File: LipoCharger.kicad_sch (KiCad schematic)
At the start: 31 parts, among them J1 S2B-XH-A, J2 USB_C_Receptacle_USB2.0_14P, Q1 2300A, Q2 2300A, SW1 SK12D07VG4, U1 TP4056-42-ESOP8, U2 MT3608, U3 FM2113

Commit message: Fixed ERC errors
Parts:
- renumbered GND1 to GND_OUT1, +5v1 to PWR_OUT1
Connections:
- net +5V: no longer names the net of C5.1, D3.1 (K), PWR_OUT1.1, R10.1
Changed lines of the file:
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@@
 	(wire
 		(pts
-			(xy 83.82 64.77) (xy 83.82 63.5)
-		)
-		(stroke
-			(width 0)
-			(type default)
-		)
-	)
-	(wire
-		(pts
 			(xy 39.37 160.02) (xy 45.72 160.02)
 		)
@@
 		(on_board yes)
 		(dnp no)
-		(property "Reference" "+5v1"
-			(at 259.588 29.464 90)
+		(property "Reference" "PWR_OUT1"
+			(at 257.302 29.464 90)
 			(effects
 				(font
@@
 			(project ""
 				(path "/b34478b6-339b-4f78-905c-fce6e8fbd016"
-					(reference "+5v1")
+					(reference "PWR_OUT1")
 					(unit 1)
 				)
@@
 	)
 	(symbol
-		(lib_id "power:+5V")
-		(at 252.73 33.02 0)
-		(unit 1)
-		(exclude_from_sim no)
-		(in_bom yes)
-		(on_board yes)
-		(dnp no)
-		(fields_autoplaced yes)
-		(property "Reference" "#PWR014"
-			(at 252.73 36.83 0)
-			(effects
-				(font
-					(size 1.27 1.27)
-				)
-				(hide yes)
-			)
-		)
-		(property "Value" "+5V"
-			(at 252.73 27.94 0)
-			(effects
-				(font
-					(size 1.27 1.27)
-				)
-			)
-		)
-		(property "Footprint" ""
-			(at 252.73 33.02 0)
-			(effects
-				(font
-					(size 1.27 1.27)
-				)
-				(hide yes)
-			)
-		)
-		(property "Datasheet" ""
-			(at 252.73 33.02 0)
-			(effects
-				(font
-					(size 1.27 1.27)
-				)
-				(hide yes)
-			)
-		)
-		(property "Description" "Power symbol creates a global label with name \"+5V\""
-			(at 252.73 33.02 0)
-			(effects
-				(font
-					(size 1.27 1.27)
-				)
-				(hide yes)
-			)
-		)
-		(pin "1"
-		)
-		(instances
-			(project ""
-				(path "/b34478b6-339b-4f78-905c-fce6e8fbd016"
-					(reference "#PWR014")
-					(unit 1)
-				)
-			)
-		)
-	)
-	(symbol
 		(lib_id "Device:R")
 		(at 147.32 31.75 0)
@@
 		(on_board yes)
 		(dnp no)
-		(property "Reference" "GND1"
-			(at 259.588 53.594 90)
+		(property "Reference" "GND_OUT1"
+			(at 257.556 53.594 90)
 			(effects
 				(font
@@
 			(project "LipoCharger"
 				(path "/b34478b6-339b-4f78-905c-fce6e8fbd016"
-					(reference "GND1")
+					(reference "GND_OUT1")
 					(unit 1)
 				)

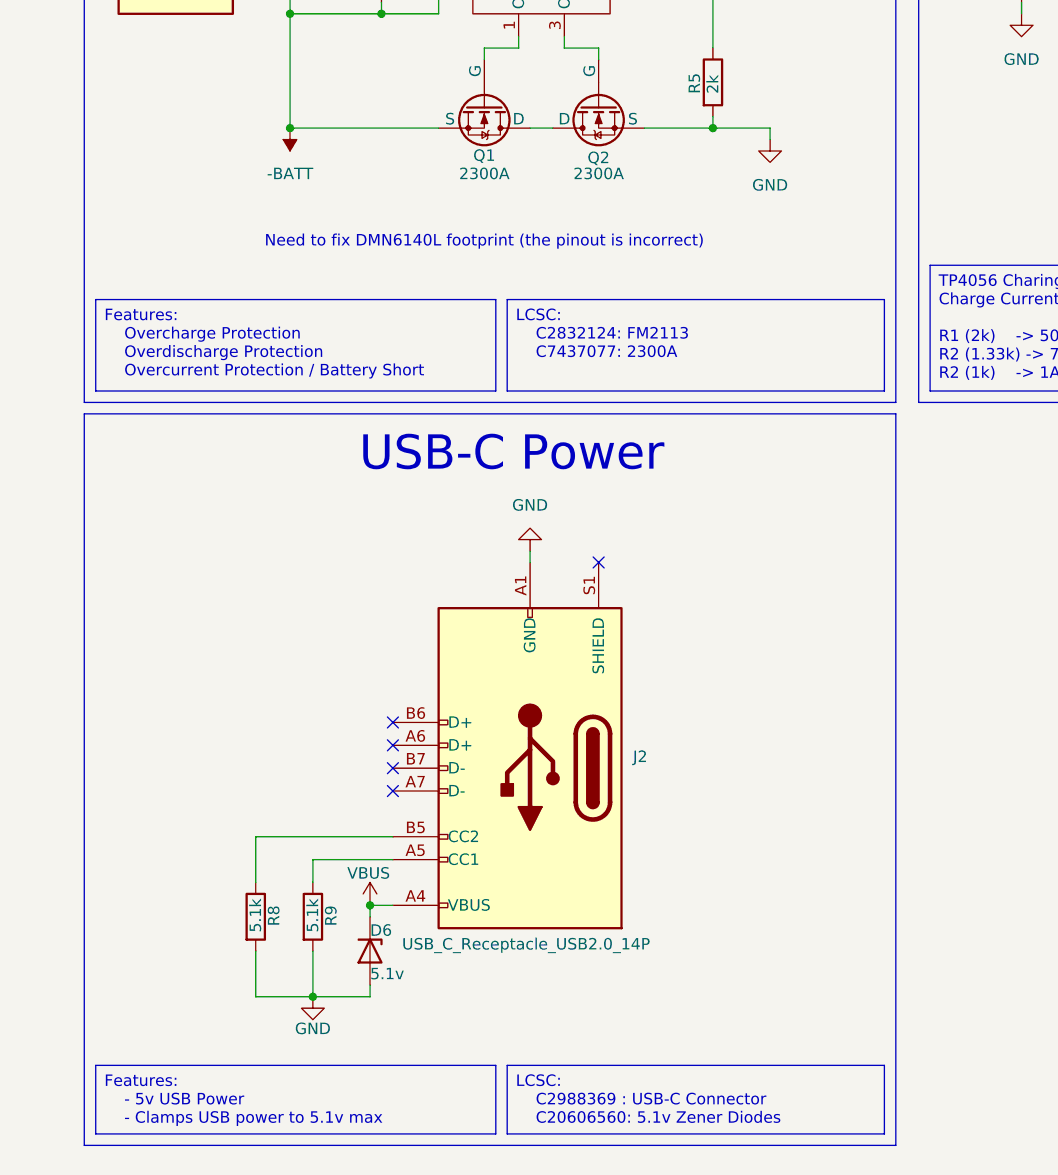
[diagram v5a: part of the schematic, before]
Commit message: updated part numbers to add stock, added part numbers to each part
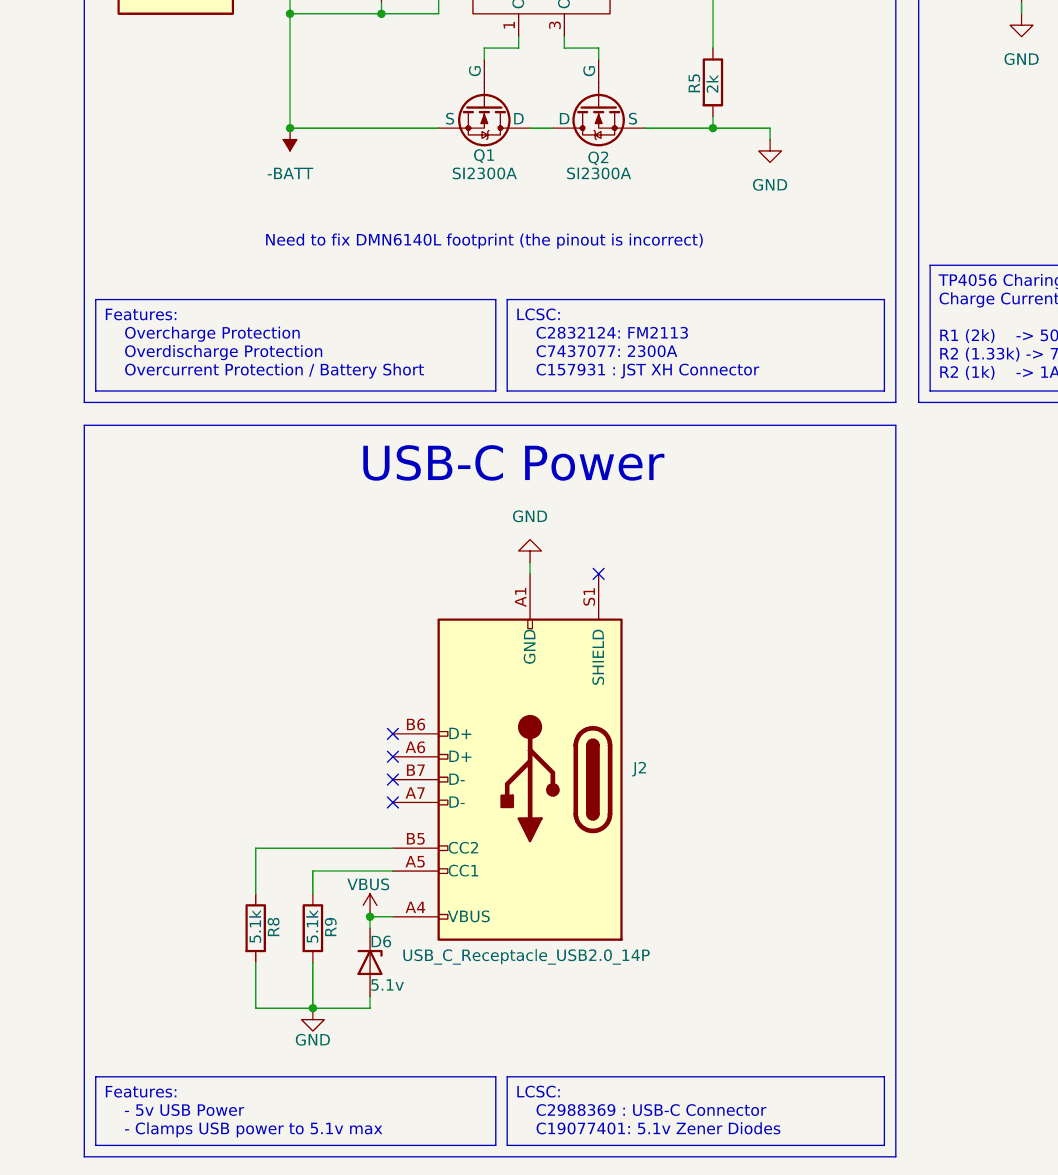
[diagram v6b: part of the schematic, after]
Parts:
- C1, C2: LCSC Part # (none) -> C19702
- C3: LCSC Part # (none) -> C14663
- C4, C5: LCSC Part # (none) -> C59461
- D1: LCSC Part # (none) -> C965799
- D2: LCSC Part # (none) -> C19171301
- D3: LCSC Part # (none) -> C908680
- D6: LCSC Part # (none) -> C19077401
- J1: LCSC Part # (none) -> C157931
- J2: LCSC Part # (none) -> C2988369
- L1: LCSC Part # (none) -> C436465
- Q1, Q2: value 2300A -> SI2300A; LCSC Part # (none) -> C347480
- R1, R5: LCSC Part # (none) -> C2907022
- R10: LCSC Part # (none) -> C2933257
- R11, R7: LCSC Part # (none) -> C98220
- R2, R3: LCSC Part # (none) -> C103198
- R4: LCSC Part # (none) -> C3016239
- R6: LCSC Part # (none) -> C5126047
- R8, R9: LCSC Part # (none) -> C3016319
- SW1: LCSC Part # (none) -> C393937
- U1: LCSC Part # (none) -> C725790
- U2: LCSC Part # (none) -> C84817
- U3: LCSC Part # (none) -> C2832124
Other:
- moved on the sheet: D6, J2, R8, R9

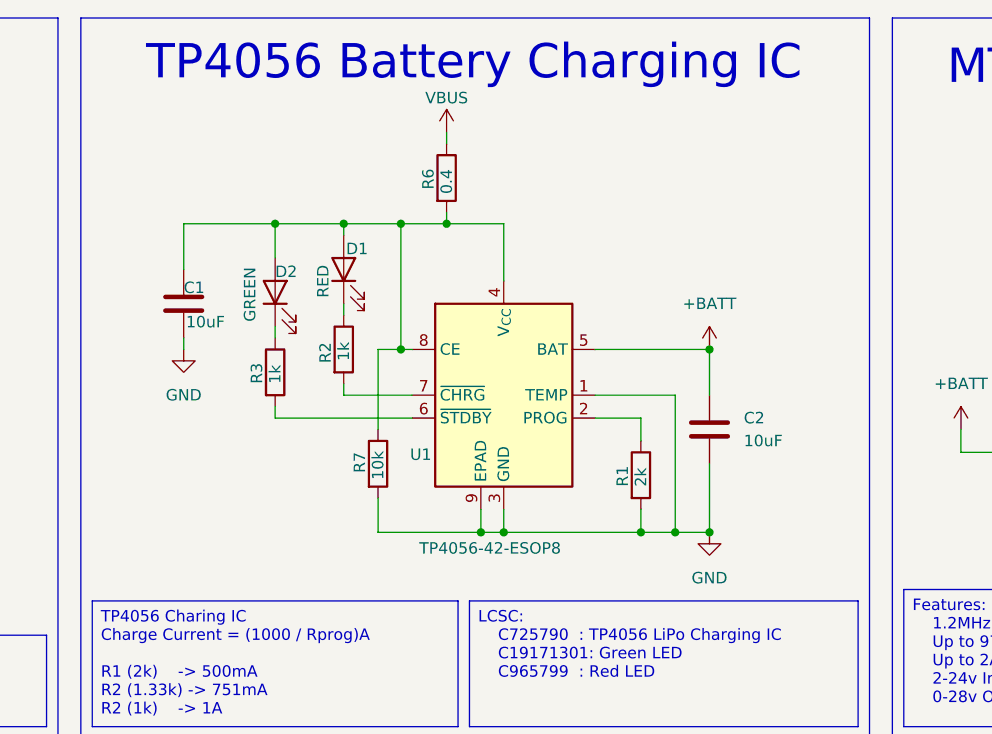
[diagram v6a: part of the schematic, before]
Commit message: Finished Layout and routing, just need to add mounting holes
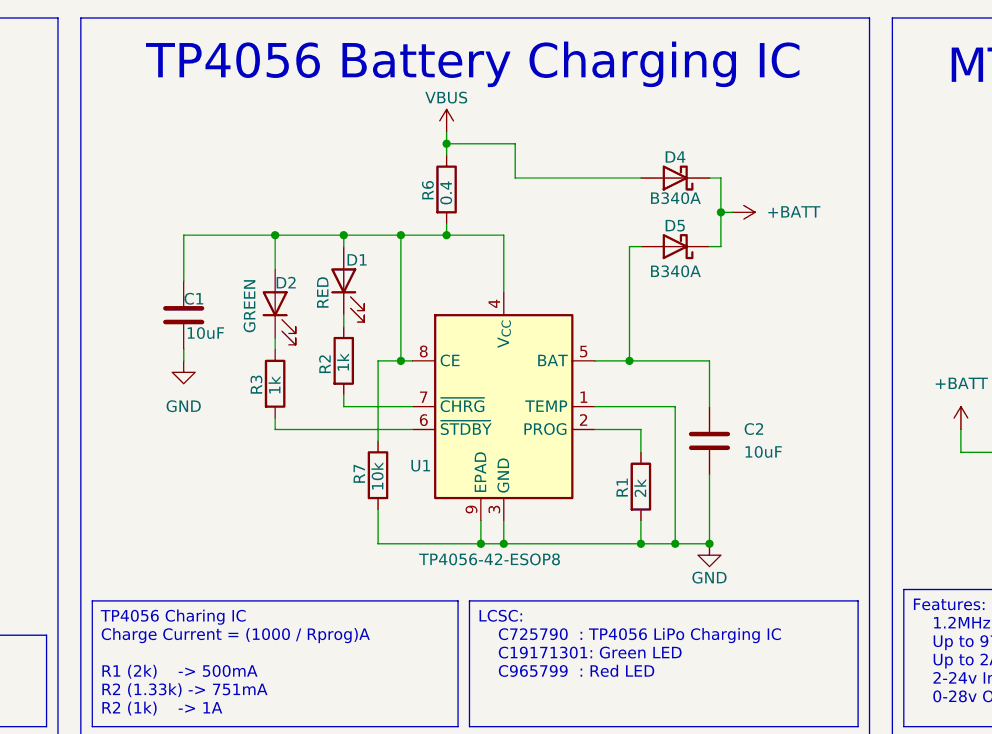
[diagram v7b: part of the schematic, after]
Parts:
- added D4, D5: B340A, Diode_SMD:D_SMA-SMB_Universal_Handsoldering, symbol Diode:B340
- L1: footprint (none) -> a_Library:WE-PD2_1054
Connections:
- net +BATT: now also D4.1 (K), D5.1 (K); no longer C2.1, U1.5 (BAT)
- net VBUS: now also D4.2 (A)
- new net: C2.1, D5.2 (A), U1.5 (BAT)
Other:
- moved on the sheet: C1, C2, D1, D2, R1, R2, R3, R6, R7, U1

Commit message: Updated to add power pathing for usb and charging ic
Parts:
- removed C4: 22uF, Capacitor_SMD:C_0603_1608Metric_Pad1.08x0.95mm_HandSolder, symbol Device:C
- removed D4, D5: B340A, Diode_SMD:D_SMA-SMB_Universal_Handsoldering, symbol Diode:B340
- removed R7: 10k, Resistor_SMD:R_0603_1608Metric_Pad0.98x0.95mm_HandSolder, symbol Device:R
- added C6, C7: 100nF, Capacitor_SMD:C_0603_1608Metric_Pad1.08x0.95mm_HandSolder, symbol Device:C
- added C8: 22uF, Capacitor_SMD:C_0603_1608Metric_Pad1.08x0.95mm_HandSolder, symbol Device:C
- added D4: MBR230LSFT1G, symbol Device:D
- added Q3: PMOS, symbol Simulation_SPICE:PMOS
- C1, C2: value 10uF -> 22uF
- C3: value 0.1uF -> 100nF
- D3: value SS34 -> MBR230LSFT1G; LCSC Part # C908680 -> C5377812
- L1: value 22uH -> 10uH; LCSC Part # C436465 -> C42931138
- R10: value 73.2k -> 82k; LCSC Part # C2933257 -> C137678
- R11: value 10k -> 11k
- R6: value 0.4 -> 10k; footprint Resistor_SMD:R_0603_1608Metric_Pad0.98x0.95mm_HandSolder -> (none); LCSC Part # C5126047 -> (none)
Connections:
- net +BATT: now also C2.1, U1.5 (BAT), Q3.1 (D); no longer L1.1, U2.5 (IN)
- net GND: now also R6.1, C6.2, C7.2, C8.2
- net VBUS: now also C1.1, D1.2 (A), D2.2 (A), R6.2, U1.4 (V_{CC}), U1.8 (CE), C6.1, D4.2 (A), Q3.2 (G); no longer R6.1
- net at C5.1, D3.1 (K), PWR_OUT1.1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: now also C8.1
- new net: C7.1, D4.1 (K), L1.1, Q3.3 (S), U2.5 (IN)
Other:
- moved on the sheet: C1, C2, C5, D1, D2, D3, GND_OUT1, L1, PWR_OUT1, R1, R10, R11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
